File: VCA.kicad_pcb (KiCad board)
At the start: 2 copper layers, 70 x 70 mm, 44 parts, among them J1 Output, J10 Conn_01x05_Male, J11 Conn_01x05_Male, J12 Conn_01x05_Male, J2 Input, J3 Env, J4 Conn_01x05_Male, J5 Conn_01x05_Male, J6 Conn_01x05_Male, J7 Conn_01x05_Male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

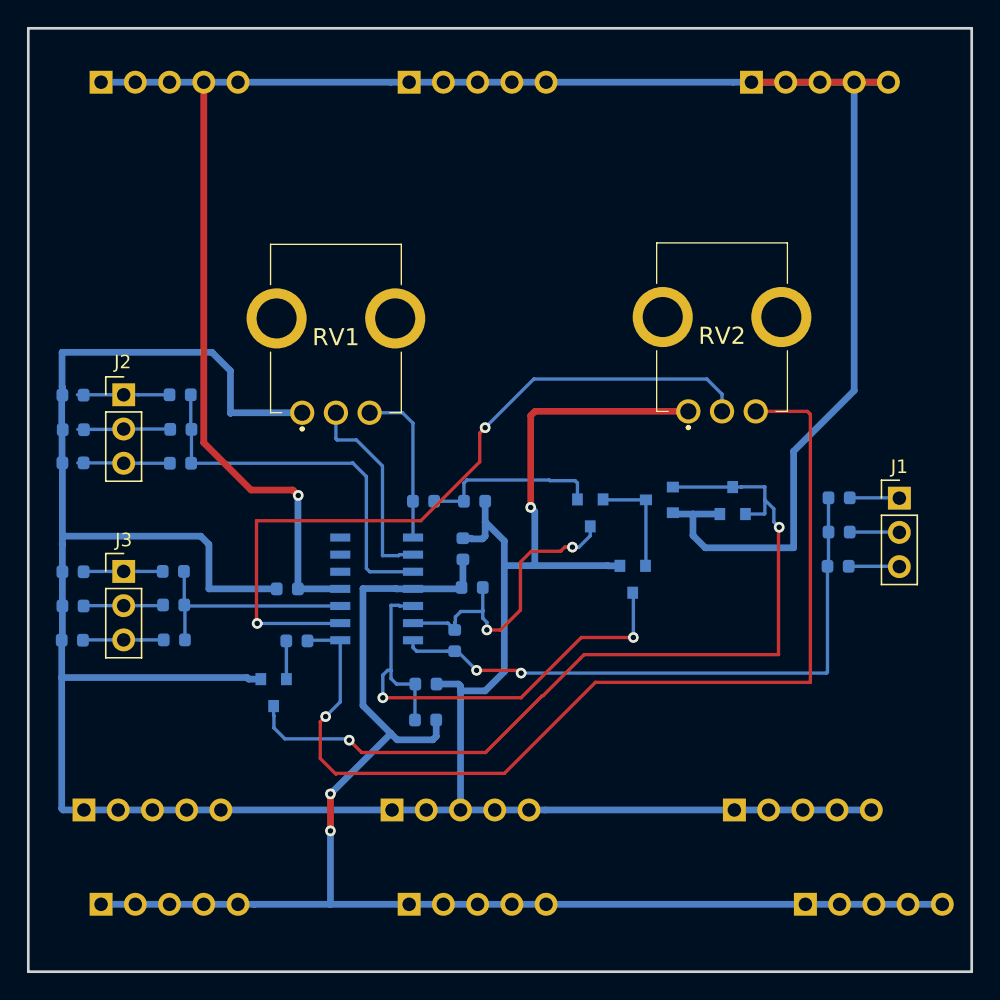
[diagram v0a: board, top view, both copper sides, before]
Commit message: Плата 40х70 мм. Добавленны подписи компонентов и регуляторов Косметические изменения в схеме, уменьшенно количество разъемов питания
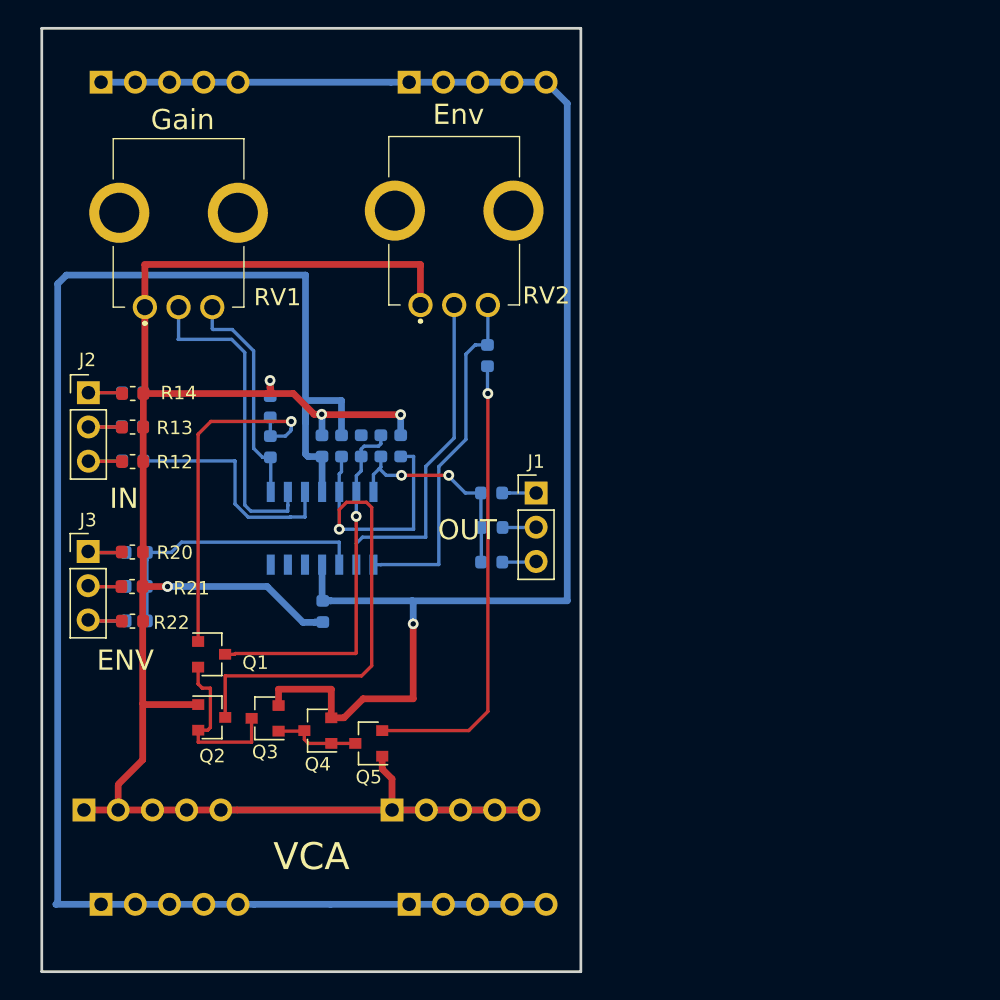
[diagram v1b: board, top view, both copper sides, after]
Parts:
- removed J11, J4, J7: Conn_01x05_Male, footprint:pls1x05
- Q1, Q2, Q3, Q4, Q5, R12, R13, R14, R20, R21, R22: moved to F.Cu
- moved Q4 35.2 mm to (41.5, 72.1), turned to 180 degrees
- moved Q3 33.4 mm to (37.6, 71.2)
- moved Q2 32.9 mm to (33.6, 71.1), turned to 0 degrees
- moved Q1 30.0 mm to (33.6, 66.5), turned to 0 degrees
- moved J1 27.0 mm to (57.7, 54.5)
- moved R4 25.8 mm to (54.4, 54.5)
- moved R6 25.8 mm to (54.4, 57.0)
- moved R8 25.7 mm to (54.4, 59.6)
- moved R17 25.5 mm to (54.1, 44.3), turned to 90 degrees
- moved RV2 21.4 mm to (51.6, 34.9)
- moved R3 21.3 mm to (43.2, 51.0), turned to 270 degrees
- moved R11 17.8 mm to (47.6, 51.0), turned to 90 degrees
- moved R15 16.7 mm to (38.0, 48.1), turned to 90 degrees
- moved R1 15.5 mm to (46.2, 51.0)
- moved RV1 14.1 mm to (31.1, 35.1)
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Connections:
- net GNDREF renamed GND
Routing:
- net Net-(Q3-Pad1): track 65.0 -> 6.49 mm, vias 2 -> 0
- net Net-(R17-Pad2): track 75.5 -> 26.2 mm, vias 1 -> 0
- net -5V: track 163.4 -> 114.2 mm
- net GND: track 212.5 -> 168.3 mm, vias 1 -> 4
- net Net-(Q5-Pad2): track 2.84 -> 34.1 mm, vias 0 -> 1
- net Net-(RV2-Pad2): track 55.7 -> 25.0 mm, vias 2 -> 0
- net Net-(R1-Pad1): track 45.1 -> 16.4 mm
- net +5V: track 102.9 -> 125.2 mm, vias 2 -> 0
- net Net-(Q1-Pad1): track 13.4 -> 26.5 mm, vias 0 -> 1
- net Net-(Q2-Pad3): track 38.0 -> 47.6 mm, vias 2 -> 1
- net Net-(RV1-Pad2): track 15.2 -> 23.9 mm
- net Net-(R10-Pad1): track 28.9 -> 22.5 mm
- net Net-(Q1-Pad2): track 8.10 -> 12.8 mm
- net Net-(R9-Pad2): track 12.0 -> 16.7 mm
- net Net-(R16-Pad1): track 16.7 -> 21.3 mm
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- added copper zone on B.Cu, net GND
- added copper zone on F.Cu, net GND
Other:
- board size 70 x 70 mm -> 40 x 70 mm
- board text added: "ENV"
- board text added: "Env"
- board text added: "Gain"
- board text added: "IN"
- board text added: "OUT"
- board text added: "VCA"
